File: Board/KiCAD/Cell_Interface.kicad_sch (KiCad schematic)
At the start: 26 parts, among them Q23 2N7002, Q24 2N7002, Q25 2N7002, Q26 2N7002, Q5 BSS83P, Q6 BSS83P, Q7 BSS83P, Q8 BSS83P, U6 INA219AxDCN, U7 INA219AxDCN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

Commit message: Team #6 - Battery Management Module Rev 1 - PCB
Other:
- note added: "Battery connections 4Cell batteries in series"
- note removed: "LTC chip does voltage, current"
- note removed: "To battey cells 1, 2, 3, or 4 cells"
- moved on the sheet: Q26, Q5, R65, R69, R72

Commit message: Edits to PCB
@andrewgreenberg @KeytarGoblin
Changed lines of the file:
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@@
 	)
 	(junction
-		(at 110.49 40.64)
-		(diameter 0)
-		(color 0 0 0 0)
-	)
-	(junction
 		(at 93.98 40.64)
 		(diameter 0)
@@
 	(wire
 		(pts
-			(xy 93.98 40.64) (xy 110.49 40.64)
-		)
-		(stroke
-			(width 0)
-			(type default)
-		)
-	)
-	(wire
-		(pts
 			(xy 80.01 160.02) (xy 80.01 157.48)
 		)
@@
 	(wire
 		(pts
-			(xy 110.49 107.95) (xy 128.27 107.95)
-		)
-		(stroke
-			(width 0)
-			(type default)
-		)
-	)
-	(wire
-		(pts
 			(xy 64.77 109.22) (xy 64.77 113.03)
 		)
@@
 	(wire
 		(pts
-			(xy 110.49 40.64) (xy 110.49 107.95)
-		)
-		(stroke
-			(width 0)
-			(type default)
-		)
-	)
-	(wire
-		(pts
 			(xy 35.56 127) (xy 35.56 121.92)
 		)
@@
 	(wire
 		(pts
-			(xy 110.49 34.29) (xy 110.49 40.64)
+			(xy 93.98 34.29) (xy 93.98 40.64)
 		)
 		(stroke
@@
 	(hierarchical_label "BATT"
 		(shape input)
-		(at 110.49 34.29 90)
+		(at 93.98 34.29 0)
 		(effects
 			(font
@@
 		)
 	)
-	(hierarchical_label "Cell 4"
-		(shape input)
-		(at 128.27 107.95 0)
-		(effects
-			(font
-				(size 1.27 1.27)
-			)
-			(justify left)
-		)
-	)
 	(hierarchical_label "SCL"
 		(shape input)
@@
 	)
 	(symbol
+		(lib_name "INA219AxDCN_1")
 		(lib_id "Sensor_Energy:INA219AxDCN")
 		(at 50.8 77.47 0)

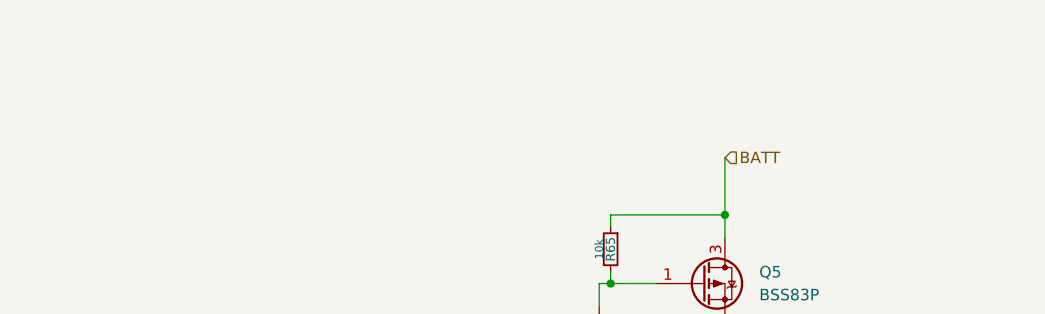
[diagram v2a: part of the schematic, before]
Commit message: Fixed Library paths for component symbol
@andrewgreenberg @KeytarGoblin
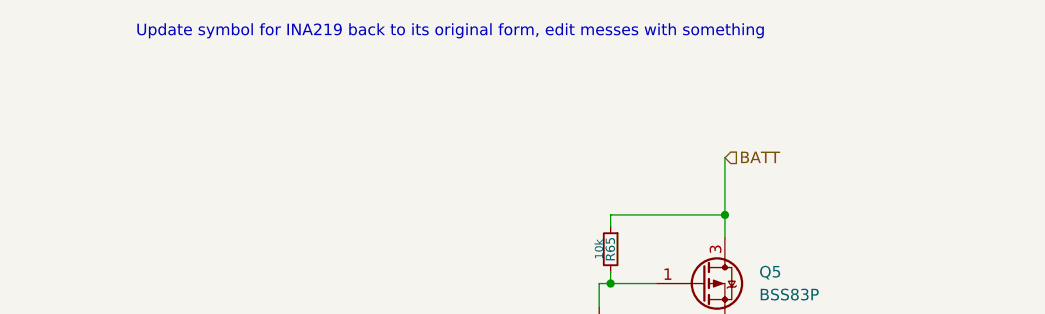
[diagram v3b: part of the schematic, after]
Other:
- note added: "Update symbol for INA219 back to its original form, edit messes with something"
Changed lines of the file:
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@@
+		)
+	)
+	(text "Update symbol for INA219 back to its original form, edit messes with something "
+		(exclude_from_sim no)
+		(at 63.5 20.32 0)
+		(effects
+			(font
+				(size 1.27 1.27)
+			)
 		)
 	)

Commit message: PCB Revision
PCN near full completion, currently running on no errors while running DRC.

@KeytarGoblin @andrewgreenberg @Danish2PSU
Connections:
- net 3.3V: now also U6.4 (VS), U6.8 (A1), U7.4 (VS), U7.7 (A0), U8.4 (VS); no longer U6.1 (A1), U6.5 (VS), U7.2 (A0), U7.5 (VS), U8.5 (VS)
- net Cell 1: now also U8.1 (IN+), U8.2 (IN-); no longer U8.7 (IN-), U8.8 (IN+)
- net Cell 2: now also U7.1 (IN+), U7.2 (IN-); no longer U7.7 (IN-), U7.8 (IN+)
- net Cell 3: now also U6.1 (IN+), U6.2 (IN-); no longer U6.7 (IN-), U6.8 (IN+)
- net GND: now also U6.3 (GND), U6.7 (A0), U7.3 (GND), U7.8 (A1), U8.3 (GND), U8.7 (A0), U8.8 (A1); no longer U6.2 (A0), U6.6 (GND), U7.1 (A1), U7.6 (GND), U8.1 (A1), U8.2 (A0), U8.6 (GND)
- net SCL: now also U6.5 (SCL), U7.5 (SCL), U8.5 (SCL); no longer U6.4 (SCL), U7.4 (SCL), U8.4 (SCL)
- net SDA: now also U6.6 (SDA), U7.6 (SDA), U8.6 (SDA); no longer U6.3 (SDA), U7.3 (SDA), U8.3 (SDA)
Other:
- note added: "0x40"
- note added: "0x41"
- note added: "0x44"
- note removed: "Address: 0x40"
- note removed: "Address: 0x41"
- note removed: "Address: 0x44"
- moved on the sheet: C47, C49, C50

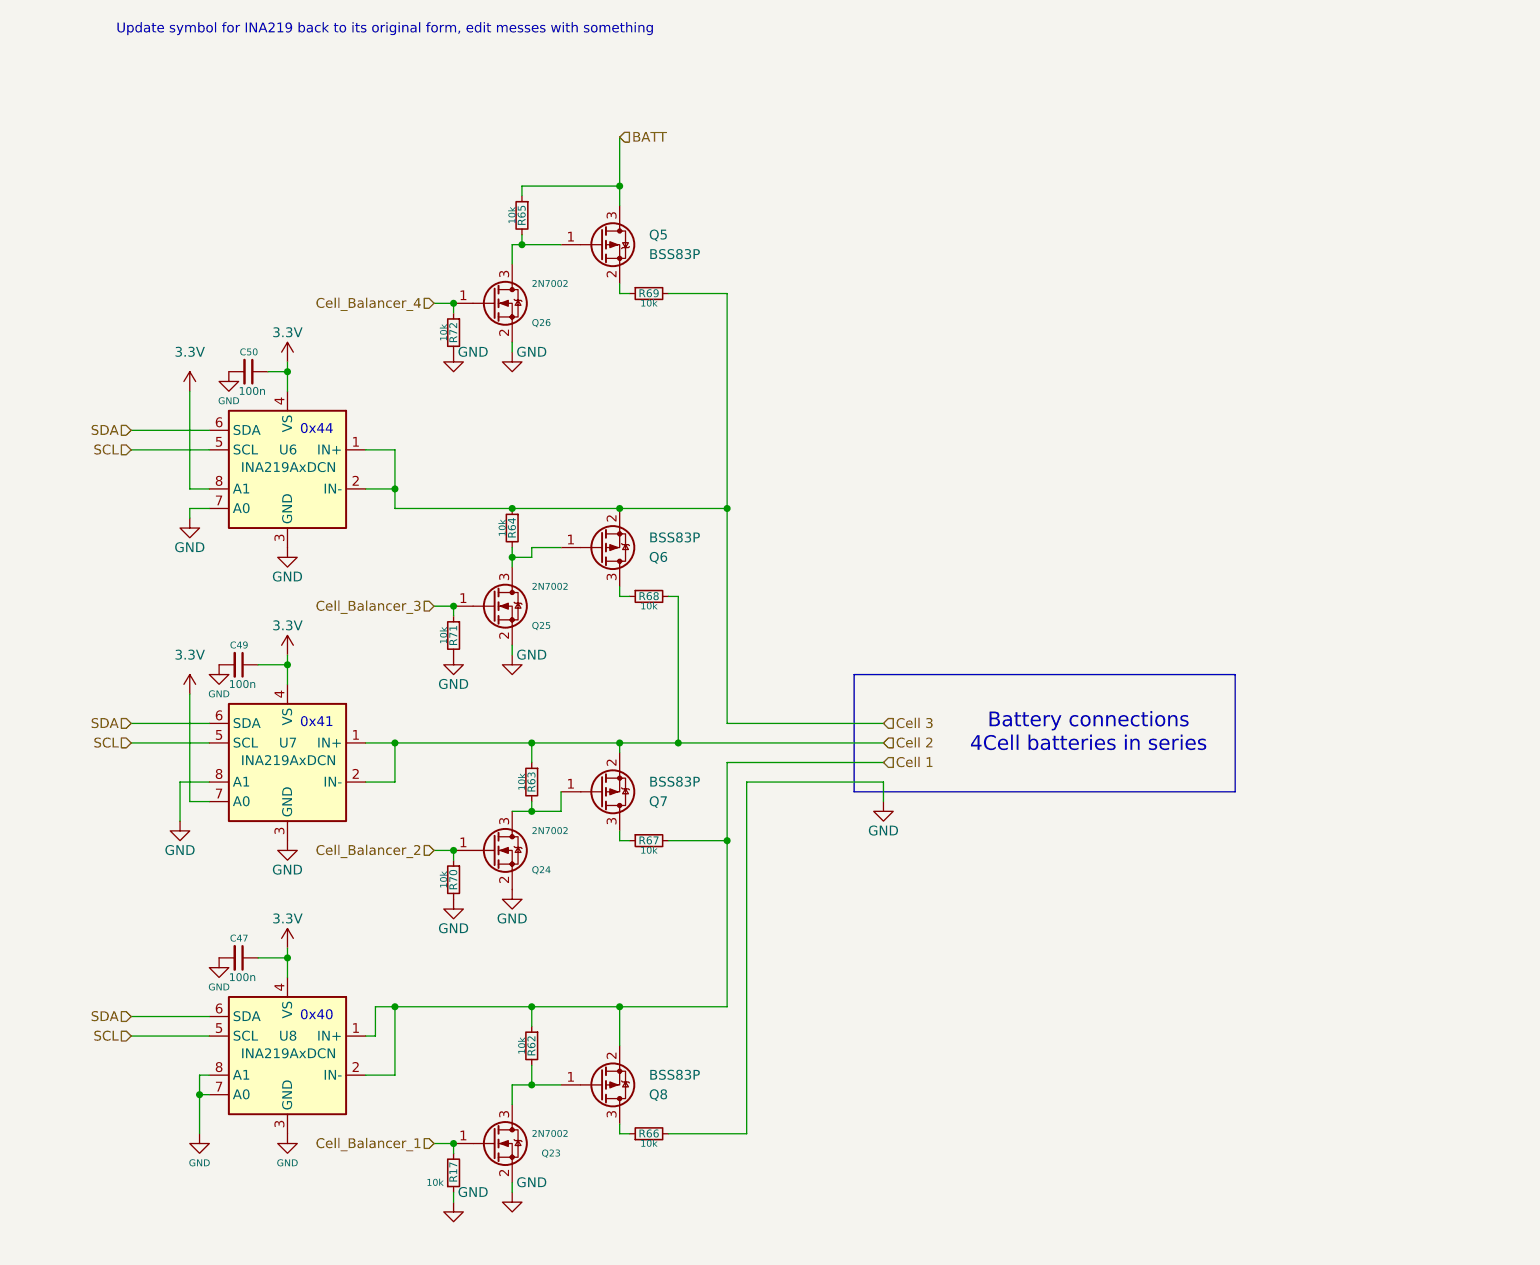
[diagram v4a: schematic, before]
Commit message: Polish on schematic and board. Changed balance resistors to 100 ohms. Lots of silly OCD cleanup and documentation. Board has thicker (0.2mm) I2C lines, cleaned up 3.3V connections to reduce impedance, lots of other small tweaks.
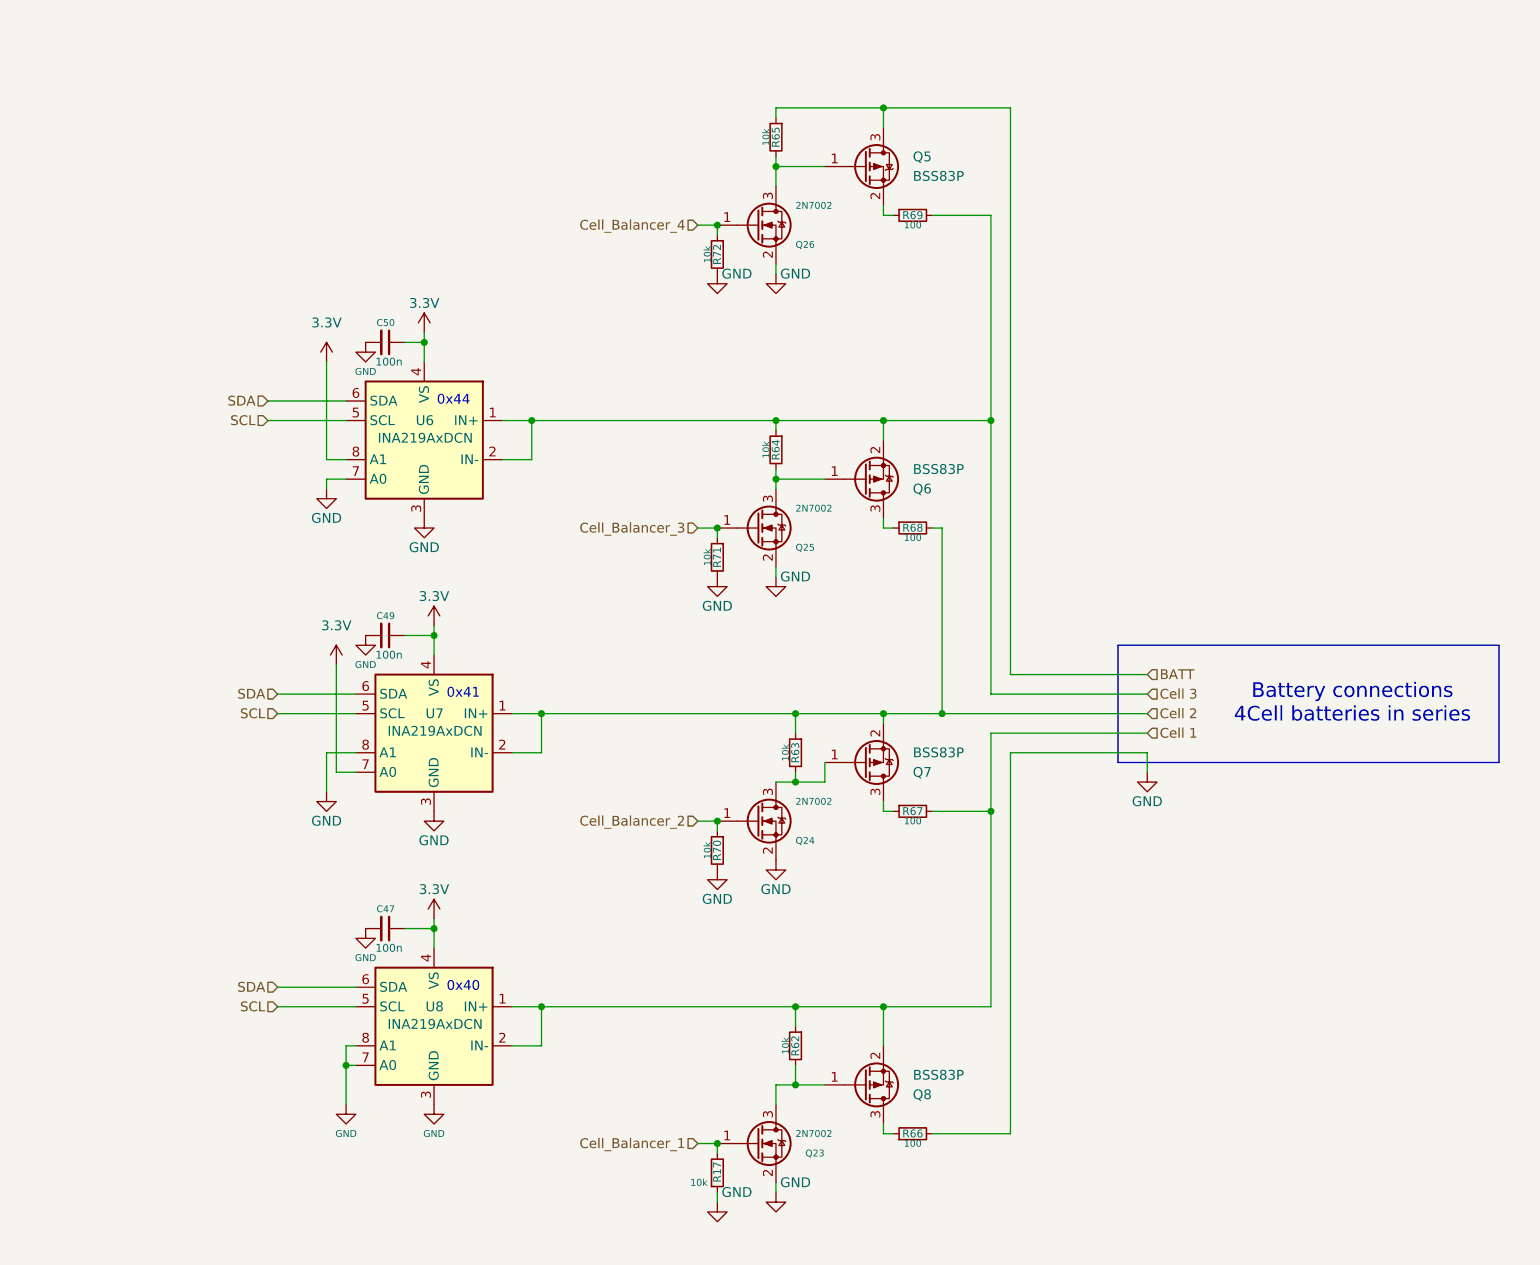
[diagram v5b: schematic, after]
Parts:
- R66, R67, R68, R69: value 10k -> 100
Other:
- note removed: "Update symbol for INA219 back to its original form, edit messes with something"
- moved on the sheet: C47, C49, C50, Q23, Q24, Q25, Q26, Q5, Q6, Q7, Q8, R17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

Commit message: Started updating BOM with MFR/MPN
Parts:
- Q23, Q24, Q25, Q26: MFR (none) -> Alpha & Omega Semiconductor
- R17, R62, R63, R64, R65, R70, R71, R72: MFR (none) -> Stackpole Electronics Inc; MPN (none) -> RMCF0603FT10K0
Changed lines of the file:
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@@
 			)
 		)
-		(property "SNAPEDA_PN" ""
+		(property "MFR" "Stackpole Electronics Inc"
 			(at 106.68 127 0)
 			(effects
@@
 					(size 1.27 1.27)
 				)
+				(hide yes)
+			)
+		)
+		(property "MPN" "RMCF0603FT10K0"
+			(at 106.68 127 0)
+			(effects
+				(font
+					(size 1.27 1.27)
+				)
+				(hide yes)
 			)
 		)
@@
 			)
 		)
-		(property "SNAPEDA_PN" ""
+		(property "MFR" "Stackpole Electronics Inc"
+			(at 116.84 114.3 0)
+			(effects
+				(font
+					(size 1.27 1.27)
+				)
+				(hide yes)
+			)
+		)
+		(property "MPN" "RMCF0603FT10K0"
 			(at 116.84 114.3 0)
 			(effects
@@
 					(size 1.27 1.27)
 				)
+				(hide yes)
 			)
 		)
@@
 			)
 		)
-		(property "SNAPEDA_PN" ""
-			(at 69.85 149.86 0)
-			(effects
-				(font
-					(size 1.27 1.27)
-				)
-			)
-		)
 		(pin "3"
 		)
@@
 			)
 		)
-		(property "SNAPEDA_PN" ""
-			(at 125.73 157.48 0)
-			(effects
-				(font
-					(size 1.27 1.27)
-				)
-			)
-		)
 		(pin "1"
 		)
@@
 			)
 		)
-		(property "SNAPEDA_PN" ""
+		(property "MFR" "Alpha & Omega Semiconductor"
 			(at 111.76 165.1 0)
 			(effects
@@
 					(size 1.27 1.27)
 				)
+				(hide yes)
 			)
 		)
@@
 			)
 		)
-		(property "SNAPEDA_PN" ""
-			(at 125.73 115.57 0)
-			(effects
-				(font
-					(size 1.27 1.27)
-				)
-			)
-		)
 		(pin "1"
 		)
@@
 			)
 		)
-		(property "SNAPEDA_PN" ""
-			(at 69.85 111.76 0)
-			(effects
-				(font
-					(size 1.27 1.27)
-				)
-			)
-		)
 		(pin "3"
 		)
@@
 			)
 		)
-		(property "SNAPEDA_PN" ""
+		(property "MFR" "Stackpole Electronics Inc"
+			(at 114.3 34.29 0)
+			(effects
+				(font
+					(size 1.27 1.27)
+				)
+				(hide yes)
+			)
+		)
+		(property "MPN" "RMCF0603FT10K0"
 			(at 114.3 34.29 0)
 			(effects
@@
 					(size 1.27 1.27)
 				)
+				(hide yes)
 			)
 		)
@@
 			)
 		)
-		(property "SNAPEDA_PN" ""
-			(at 132.08 85.09 0)
-			(effects
-				(font
-					(size 1.27 1.27)
-				)
-			)
-		)
 		(pin "2"
 		)
@@
 			)
 		)
-		(property "SNAPEDA_PN" ""
+		(property "MFR" "Stackpole Electronics Inc"
 			(at 106.68 168.91 0)
 			(effects
@@
 					(size 1.27 1.27)
 				)
+				(hide yes)
+			)
+		)
+		(property "MPN" "RMCF0603FT10K0"
+			(at 106.68 168.91 0)
+			(effects
+				(font
+					(size 1.27 1.27)
+				)
+				(hide yes)
 			)
 		)
@@
 			)
 		)
-		(property "SNAPEDA_PN" ""
-			(at 132.08 121.92 0)
-			(effects
-				(font
-					(size 1.27 1.27)
-				)
-			)
-		)
 		(pin "2"
 		)
@@
 			)
 		)
-		(property "SNAPEDA_PN" ""
+		(property "MFR" "Stackpole Electronics Inc"
+			(at 106.68 49.53 0)
+			(effects
+				(font
+					(size 1.27 1.27)
+				)
+				(hide yes)
+			)
+		)
+		(property "MPN" "RMCF0603FT10K0"
 			(at 106.68 49.53 0)
 			(effects
@@
 					(size 1.27 1.27)
 				)
+				(hide yes)
 			)
 		)
@@
 			)
 		)
-		(property "SNAPEDA_PN" ""
-			(at 63.5 137.16 0)
-			(effects
-				(font
-					(size 1.27 1.27)
-				)
-			)
-		)
 		(pin "1"
 		)
@@
 			)
 		)
-		(property "SNAPEDA_PN" ""
-			(at 63.5 99.06 0)
-			(effects
-				(font
-					(size 1.27 1.27)
-				)
-			)
-		)
 		(pin "1"
 		)
@@
 			)
 		)
-		(property "SNAPEDA_PN" ""
-			(at 125.73 78.74 0)
-			(effects
-				(font
-					(size 1.27 1.27)
-				)
-			)
-		)
 		(pin "1"
 		)
@@
 			)
 		)
-		(property "SNAPEDA_PN" ""
-			(at 132.08 163.83 0)
-			(effects
-				(font
-					(size 1.27 1.27)
-				)
-			)
-		)
 		(pin "2"
 		)
@@
 			)
 		)
-		(property "SNAPEDA_PN" ""
-			(at 125.73 38.1 0)
-			(effects
-				(font
-					(size 1.27 1.27)
-				)
-			)
-		)
 		(pin "1"
 		)
@@
 			)
 		)
-		(property "SNAPEDA_PN" ""
+		(property "MFR" "Stackpole Electronics Inc"
 			(at 106.68 88.9 0)
 			(effects
@@
 					(size 1.27 1.27)
 				)
+				(hide yes)
+			)
+		)
+		(property "MPN" "RMCF0603FT10K0"
+			(at 106.68 88.9 0)
+			(effects
+				(font
+					(size 1.27 1.27)
+				)
+				(hide yes)
 			)
 		)
@@
 			)
 		)
-		(property "SNAPEDA_PN" ""
-			(at 132.08 44.45 0)
-			(effects
-				(font
-					(size 1.27 1.27)
-				)
-			)
-		)
 		(pin "2"
 		)
@@
 			)
 		)
-		(property "SNAPEDA_PN" ""
+		(property "MFR" "Stackpole Electronics Inc"
+			(at 114.3 74.93 0)
+			(effects
+				(font
+					(size 1.27 1.27)
+				)
+				(hide yes)
+			)
+		)
+		(property "MPN" "RMCF0603FT10K0"
 			(at 114.3 74.93 0)
 			(effects
@@
 					(size 1.27 1.27)
 				)
+				(hide yes)
 			)
 		)
@@
 			)
 		)
-		(property "SNAPEDA_PN" ""
+		(property "MFR" "Alpha & Omega Semiconductor"
 			(at 111.76 123.19 0)
 			(effects
@@
 					(size 1.27 1.27)
 				)
+				(hide yes)
 			)
 		)
@@
 			)
 		)
-		(property "SNAPEDA_PN" ""
+		(property "MFR" "Stackpole Electronics Inc"
 			(at 116.84 152.4 0)
 			(effects
@@
 					(size 1.27 1.27)
 				)
+				(hide yes)
+			)
+		)
+		(property "MPN" "RMCF0603FT10K0"
+			(at 116.84 152.4 0)
+			(effects
+				(font
+					(size 1.27 1.27)
+				)
+				(hide yes)
 			)
 		)
@@
 			)
 		)
-		(property "SNAPEDA_PN" ""
+		(property "MFR" "Alpha & Omega Semiconductor"
 			(at 111.76 45.72 0)
 			(effects
@@
 					(size 1.27 1.27)
 				)
+				(hide yes)
 			)
 		)
@@
 			)
 		)
-		(property "SNAPEDA_PN" ""
+		(property "MFR" "Alpha & Omega Semiconductor"
 			(at 111.76 85.09 0)
 			(effects
@@
 					(size 1.27 1.27)
 				)
+				(hide yes)
 			)
 		)
@@
 			)
 		)
-		(property "SNAPEDA_PN" ""
-			(at 63.5 60.96 0)
-			(effects
-				(font
-					(size 1.27 1.27)
-				)
-			)
-		)
 		(pin "1"
 		)
@@
 			)
 		)
-		(property "SNAPEDA_PN" ""
-			(at 68.58 73.66 0)
-			(effects
-				(font
-					(size 1.27 1.27)
-				)
-			)
-		)

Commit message: Battery Management System Rev 1 Board
Completed Rev 1 PCB board
@KeytarGoblin @andrewgreenberg
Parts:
- R66, R67, R68, R69: footprint Resistor_SMD:R_0603_1608Metric -> Resistor_SMD:R_1206_3216Metric
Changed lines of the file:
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@@
 			)
 		)
-		(property "Footprint" "Resistor_SMD:R_0603_1608Metric"
+		(property "Footprint" "Resistor_SMD:R_1206_3216Metric"
 			(at 132.08 85.09 0)
 			(effects
@@
 			)
 		)
-		(property "Footprint" "Resistor_SMD:R_0603_1608Metric"
+		(property "Footprint" "Resistor_SMD:R_1206_3216Metric"
 			(at 132.08 121.92 0)
 			(effects
@@
 			)
 		)
-		(property "Footprint" "Resistor_SMD:R_0603_1608Metric"
+		(property "Footprint" "Resistor_SMD:R_1206_3216Metric"
 			(at 132.08 163.83 0)
 			(effects
@@
 			)
 		)
-		(property "Footprint" "Resistor_SMD:R_0603_1608Metric"
+		(property "Footprint" "Resistor_SMD:R_1206_3216Metric"
 			(at 132.08 44.45 0)
 			(effects

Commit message: BOM Complete Need a Once Over Check
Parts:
- C47, C49, C50: MFR (none) -> Aillen; MPN (none) -> 3372-0603B104K500XDTR-ND; Package (none) -> 0603B104K500XD
- Q23, Q24, Q25, Q26: MFR Alpha & Omega Semiconductor -> onsemi; MPN (none) -> 2N7002NCT-ND; Package (none) -> 2N7002
- Q5, Q6, Q7, Q8: MFR (none) -> Infineon Technologies; MPN (none) -> BSS83PH6327XTSA1CT-ND; Package (none) -> BSS83PH6327XTSA1
- R17, R62, R63, R64, R65, R70, R71, R72: MPN RMCF0603FT10K0 -> RMCF0603FT10K0CT-ND; Package (none) -> RMCF0603FT10K0
- R66, R67, R68, R69: MFR (none) -> Stackpole Electronics Inc; MPN (none) -> RNCF1206TKY100RCT-ND; Package (none) -> RNCF1206TKY100R
- U6, U7, U8: MFR (none) -> Texas Instruments; MPN (none) -> 296-23770-1-ND; Package (none) -> INA219AIDCNR
